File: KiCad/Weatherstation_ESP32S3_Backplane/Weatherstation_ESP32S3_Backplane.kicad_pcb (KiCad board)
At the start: 2 copper layers, 99.9 x 99.9 mm, 69 parts, among them J1 01x02 JST XH, J10 01x04 Molex KK254, J11 01x02 JST XH, J12 01x04 Molex KK254, J13 01x22 Generic socket, J14 01x22 Generic socket, J15 01x02 JST XH, J16 01x04 Molex KK254, J17 01x02 JST XH, J18 01x06 Generic socket, J19 01x06 Generic socket, J2 01x03 JST XH, J3 01x03 JST XH, J4 01x07 Generic socket, J5 01x08 Generic socket, J6 01x08 Generic socket, J7 01x04 JST XH, J8 01x04 Molex KK254, J9 282834-2 Screw Terminal, Q1 RFP12N10L, U1 LM7805, U2 MAX6675ISA+T

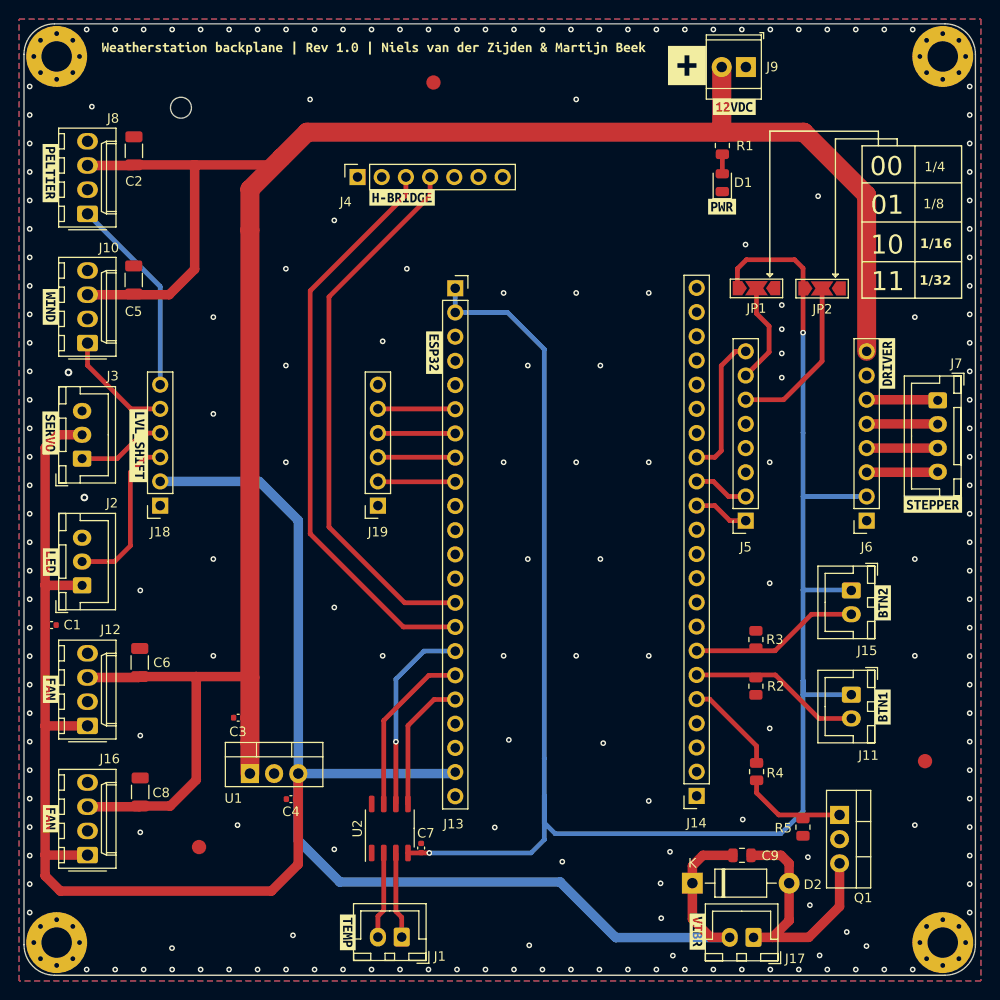
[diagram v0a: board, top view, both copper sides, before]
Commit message: Added DBG_LED, flat-mount LM7805, GPIO breakout header
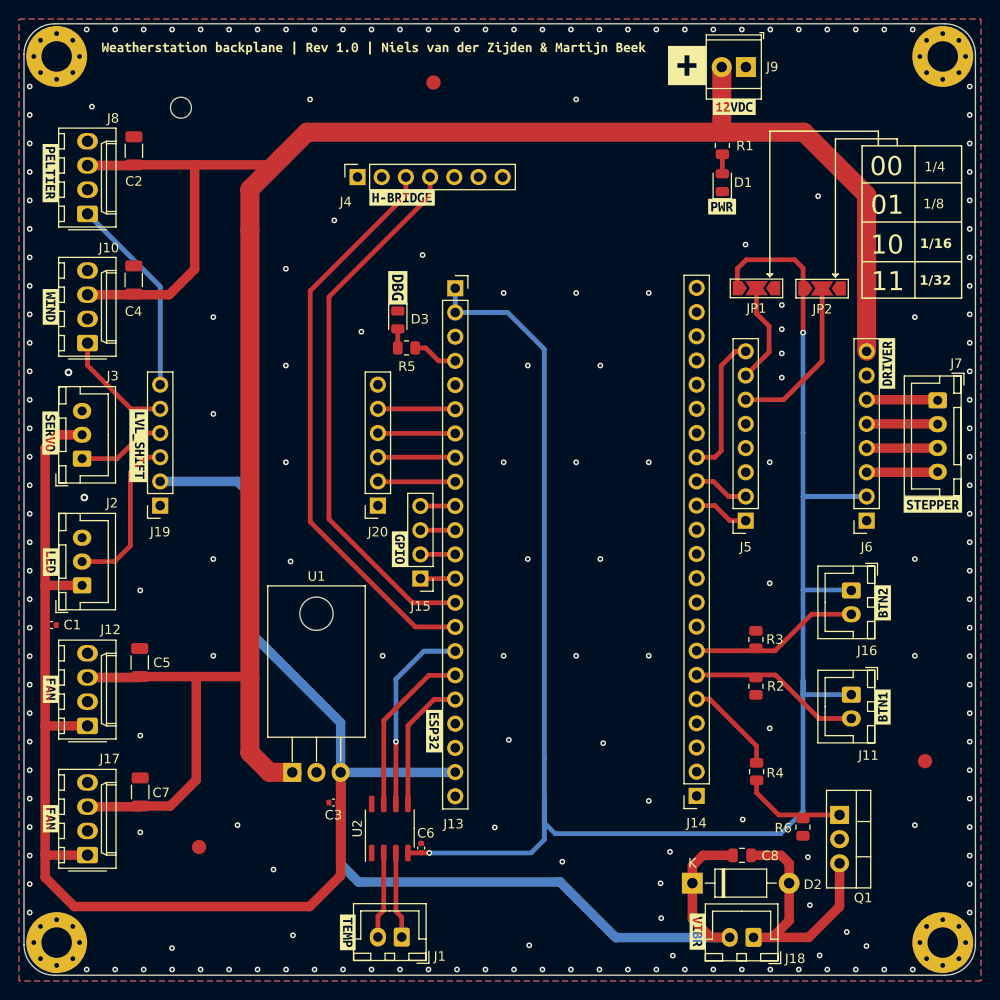
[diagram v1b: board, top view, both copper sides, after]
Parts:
- removed the C3 at (155.0, 105.6)
- added D3: DBG_LED, LED_SMD:LED_0805_2012Metric, F.Cu at (171.8, 63.8)
- added J15: 01x04 Generic header, Connector_PinHeader_2.54mm:PinHeader_1x04_P2.54mm_Vertical, F.Cu at (174.1, 91.0)
- added R5: 1k, Resistor_SMD:R_0805_2012Metric, F.Cu at (172.7, 66.7)
- added kibuzzard-6446400D: G***, kibuzzard-6446400D, F.Cu at (172.0, 87.9)
- added kibuzzard-6446408C: G***, kibuzzard-6446408C, F.Cu at (171.8, 60.4)
- U1: footprint Package_TO_SOT_THT:TO-220-3_Vertical -> Package_TO_SOT_THT:TO-220-3_Horizontal_TabDown
- moved kibuzzard-6443C88F 39.7 mm to (175.6, 107.0)
- moved C3 4.47 mm to (165.0, 114.5)
- moved U1 4.45 mm to (160.7, 111.3)
- renumbered C4 to C3, C5 to C4, C6 to C5, C7 to C6, C8 to C7, C9 to C8, J15 to J16, J16 to J17, J17 to J18, J18 to J19, J19 to J20, R5 to R6
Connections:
- J13 pad 4: /ESP_4 -> /DBG_LED
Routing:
- net /DBG_LED: track 0.00 -> 4.77 mm
- net /ESP_8: track 0.00 -> 3.66 mm
- net /ESP_3: track 0.00 -> 3.66 mm
- net /ESP_18: track 0.00 -> 3.66 mm
- net /ESP_17: track 0.00 -> 3.66 mm
- net +12V: track 239.2 -> 242.3 mm
- net Net-(D3-A): track 0.00 -> 2.00 mm
- net /D0_HEAT: track 60.9 -> 60.2 mm
